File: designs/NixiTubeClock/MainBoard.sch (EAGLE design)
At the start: 17 parts, among them IC1 LD117ADT-TR, J1 S2B-PH-SM4, J2 S2B-PH-SM4, J4 S2B-PH-SM4, J5 PJ-002AH-SMT-TR, J6 S2B-PH-SM4

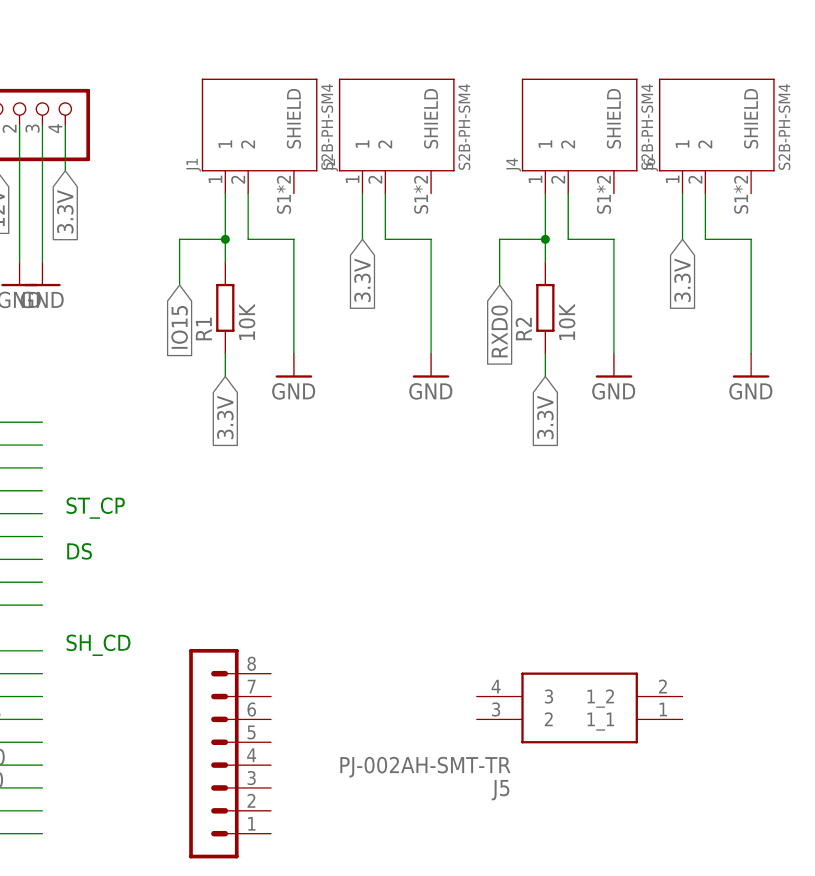
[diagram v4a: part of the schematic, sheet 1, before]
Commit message: added pinout on mainboard
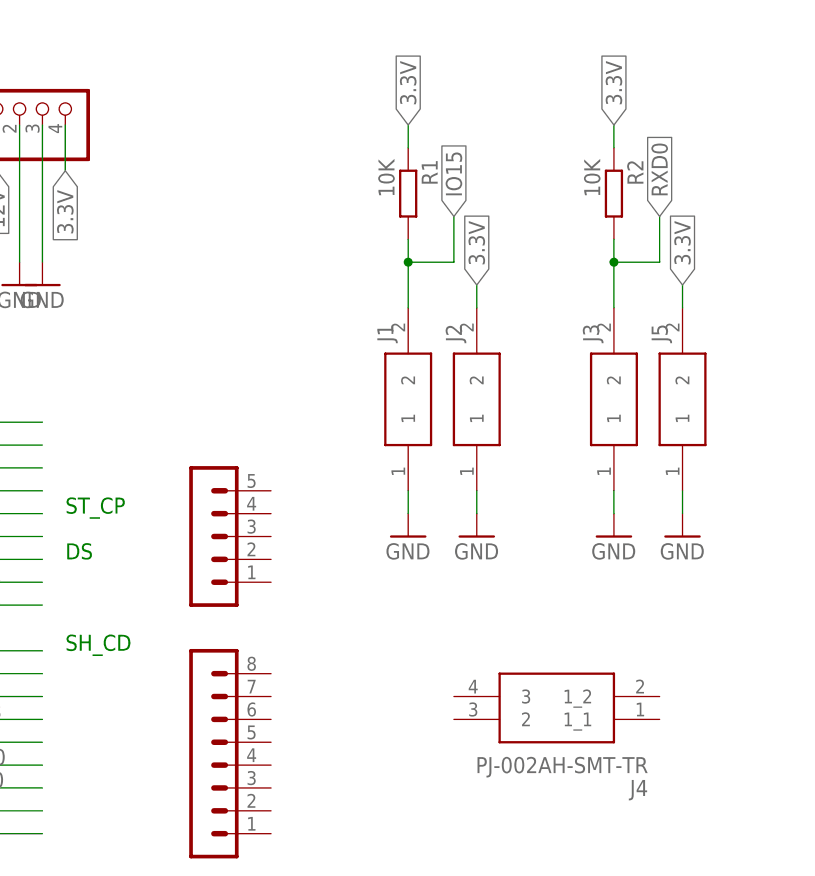
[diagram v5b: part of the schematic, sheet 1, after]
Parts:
- removed J6: S2B-PH-SM4, CommonParts:S2B-PH-SM4
- added J3: S2B-NSHSS-TB, CommonParts:S2B-NSHSS-TB
- added SV7: (no value), CommonParts:PINHEADER-1X8
- J1, J2: value S2B-PH-SM4 -> S2B-NSHSS-TB; device CommonParts:S2B-PH-SM4 -> CommonParts:S2B-NSHSS-TB
- J4: value S2B-PH-SM4 -> PJ-002AH-SMT-TR; device CommonParts:S2B-PH-SM4 -> CommonParts:PJ-002AH-SMT-TR
- J5: value PJ-002AH-SMT-TR -> S2B-NSHSS-TB; device CommonParts:PJ-002AH-SMT-TR -> CommonParts:S2B-NSHSS-TB
- SV6: device CommonParts:PINHEADER-1X8 -> con-lstb:MA05-1
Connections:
- net 3.3V: now also J2.2, J5.2; no longer J2.1, J6.1
- net GND: now also J1.1, J2.1, J3.1, J5.1; no longer J1.2, J2.2, J4.2, J6.2
- net IO15: now also J1.2; no longer J1.1
- net RXD0: now also J3.2; no longer J4.1
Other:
- moved on the sheet: R1, R2

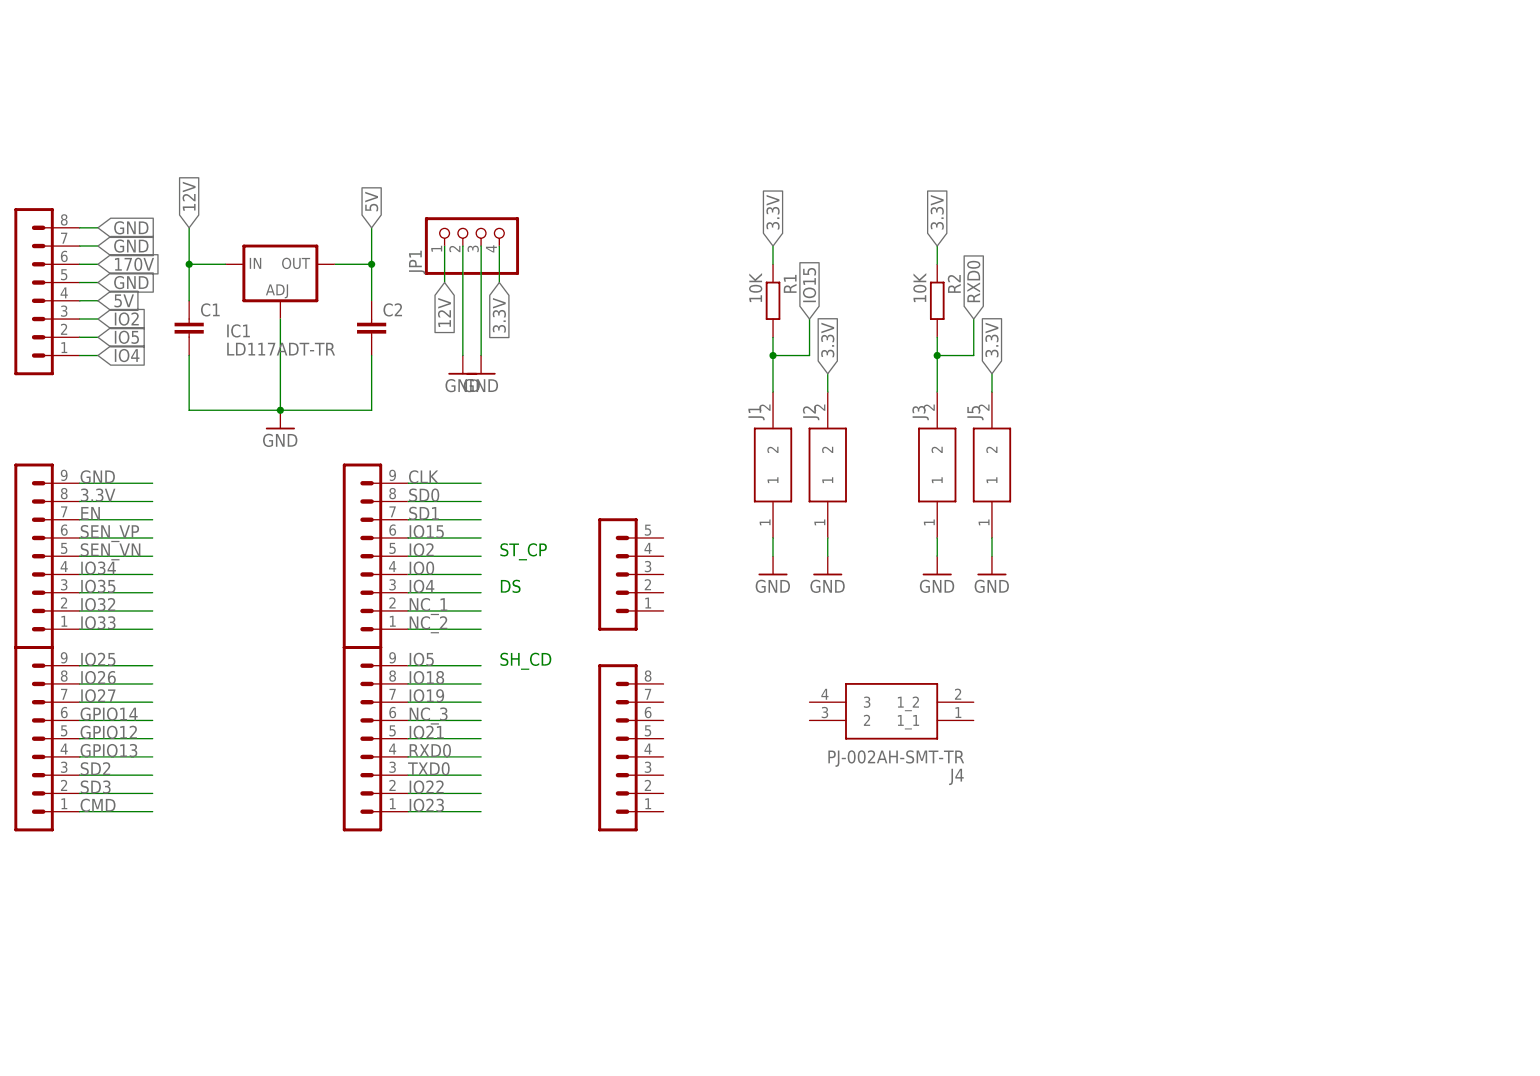
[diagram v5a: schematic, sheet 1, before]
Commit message: added work to mainboard LEDs N-Channel Mosfet and names tNames
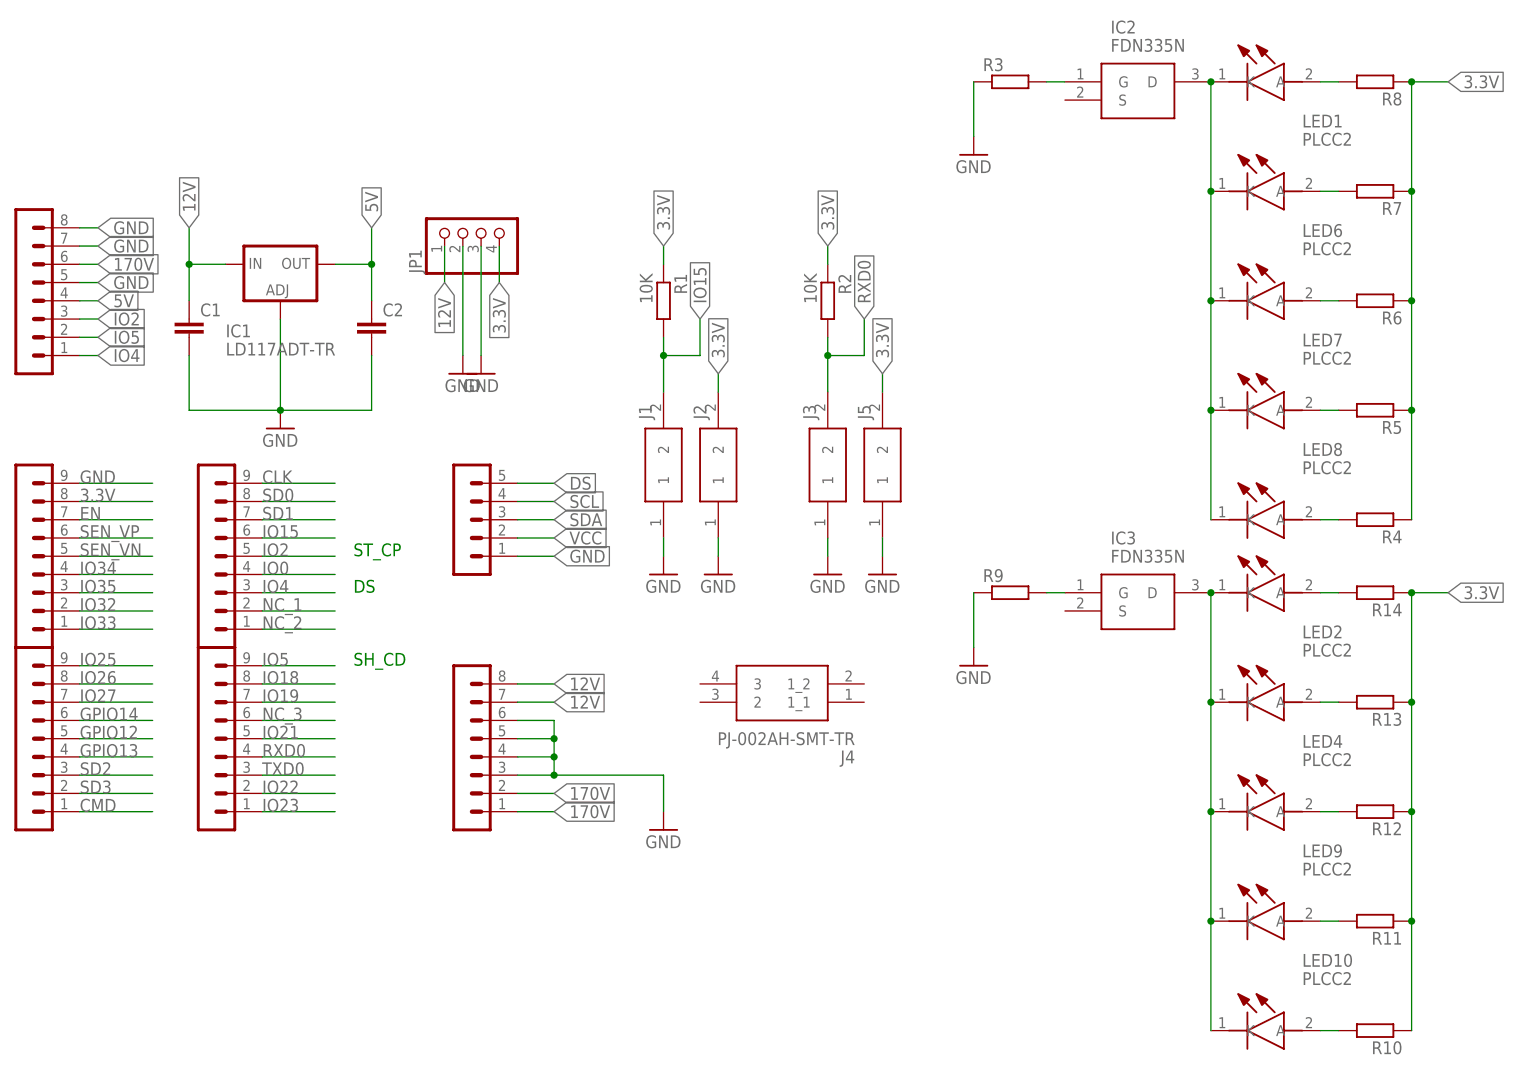
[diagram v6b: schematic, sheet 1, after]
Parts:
- added IC2, IC3: FDN335N, CommonParts:FDN335N
- added LED1, LED10, LED2, LED3, LED4, LED5, LED6, LED7, LED8, LED9: PLCC2, CommonParts:PLCC2
- added R10, R11, R12, R13, R14, R3, R4, R5, R6, R7, R8, R9: (no value), CommonParts:R-EU_1206R1206
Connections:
- new net DS: SV6.5
- new net N$1: IC2.D, LED1.K, LED5.K, LED6.K, LED7.K, LED8.K
- new net N$10: LED3.A, R14.2
- new net N$11: LED2.A, R13.2
- new net N$12: LED4.A, R12.2
- new net N$13: LED9.A, R11.2
- new net N$14: LED10.A, R10.2
- new net N$2: IC2.G, R3.2
- new net N$3: LED5.A, R8.2
- new net N$4: LED1.A, R7.2
- new net N$5: LED6.A, R6.2
- new net N$6: LED7.A, R5.2
- new net N$7: LED8.A, R4.2
- new net N$8: IC3.G, R9.2
- new net N$9: IC3.D, LED10.K, LED2.K, LED3.K, LED4.K, LED9.K
- new net SCL: SV6.4
- new net SDA: SV6.3
- new net VCC: SV6.2
- net 12V: now also SV7.7, SV7.8
- net 170V: now also SV7.1, SV7.2
- net 3.3V: now also R10.1, R11.1, R12.1, R13.1, R14.1, R4.1, R5.1, R6.1, R7.1, R8.1
- net GND: now also R3.1, R9.1, SV6.1, SV7.3, SV7.4, SV7.5, SV7.6
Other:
- moved on the sheet: J1, J2, J3, J4, J5, R1, R2

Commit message: added nixiClock brd and sheet with new design OSH
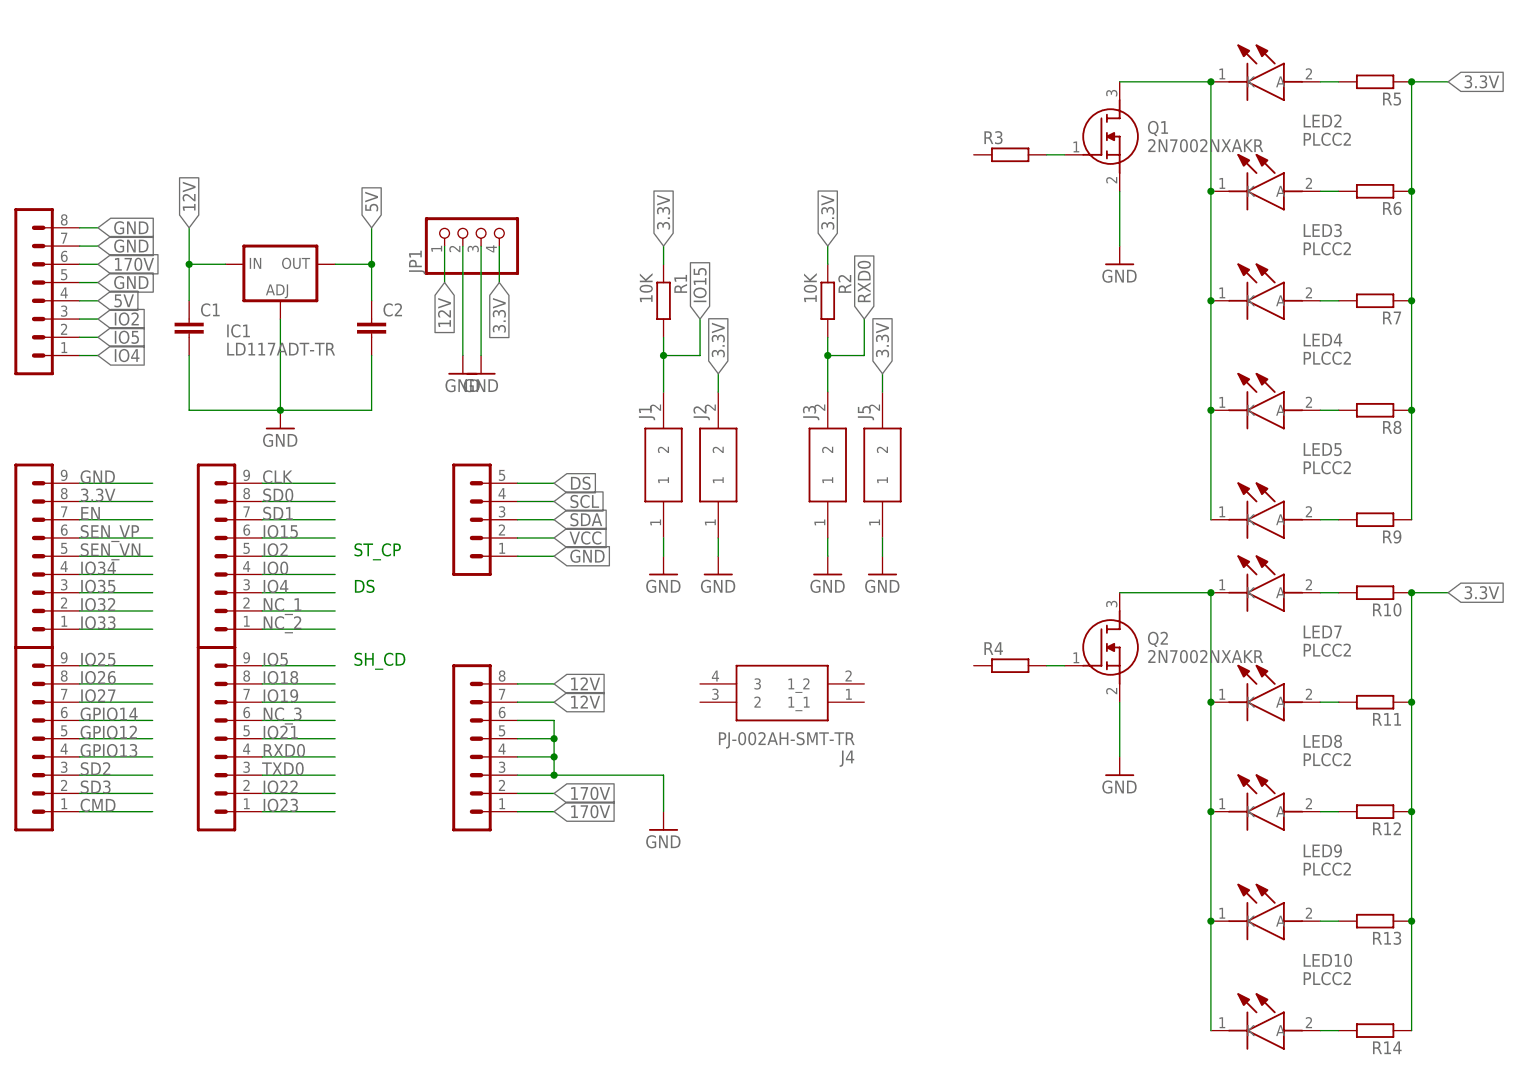
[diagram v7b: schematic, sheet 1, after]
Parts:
- removed IC2, IC3: FDN335N, CommonParts:FDN335N
- added Q1, Q2: 2N7002NXAKR, CommonParts:2N7002NXAKR
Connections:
- removed net N$1: IC2.D, LED1.K, LED5.K, LED6.K, LED7.K, LED8.K
- new net N$28: LED1.K, LED2.K, LED3.K, LED4.K, LED5.K, Q1.D
- net 3.3V: now also R9.1; no longer R4.1
- net GND: now also Q1.S, Q2.S; no longer R3.1, R9.1
- net N$10: now also LED6.A, R10.2; no longer LED3.A, R14.2
- net N$11: now also LED7.A, R11.2; no longer LED2.A, R13.2
- net N$12: now also LED8.A; no longer LED4.A
- net N$13: now also R13.2; no longer R11.2
- net N$14: now also R14.2; no longer R10.2
- net N$2: now also Q1.G; no longer IC2.G
- net N$3: now also LED1.A, R5.2; no longer LED5.A, R8.2
- net N$4: now also LED2.A, R6.2; no longer LED1.A, R7.2
- net N$5: now also LED3.A, R7.2; no longer LED6.A, R6.2
- net N$6: now also LED4.A, R8.2; no longer LED7.A, R5.2
- net N$7: now also LED5.A, R9.2; no longer LED8.A, R4.2
- net N$8: now also Q2.G, R4.2; no longer IC3.G, R9.2
- net N$9: now also LED6.K, LED7.K, LED8.K, Q2.D; no longer IC3.D, LED2.K, LED3.K, LED4.K
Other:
- moved on the sheet: LED2, LED4, LED7, LED8, R10, R11, R13, R14, R3, R4, R5, R6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

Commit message: integrated T/H sensor
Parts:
- added C3, C4: 20nF, CommonParts:C-EU_805C0805
- added JP2: (no value), pinhead:PINHD-1X4
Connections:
- removed net SCL: SV6.4
- removed net SDA: SV6.3
- removed net VCC: SV6.2
- net 12V: now also J4.2, J4.3
- net 3.3V: now also JP2.1, SV6.2
- net GND: now also C3.2, C4.2, J4.1_1, J4.1_2, JP2.2
- net IO15: now also C3.1
- net IO21: now also JP2.4, SV6.3
- net IO22: now also JP2.3, SV6.4
- net IO26: now also R3.1
- net IO27: now also R4.1
- net RXD0: now also C4.1
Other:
- note added: "SCL"
- note added: "SDA"
- moved on the sheet: J1, J2, J3, J4, J5, LED2, LED3, LED4, LED5, R1, R2, R6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
